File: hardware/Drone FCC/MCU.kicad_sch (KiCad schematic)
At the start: 5 parts, among them U3 STM32F746ZGTx

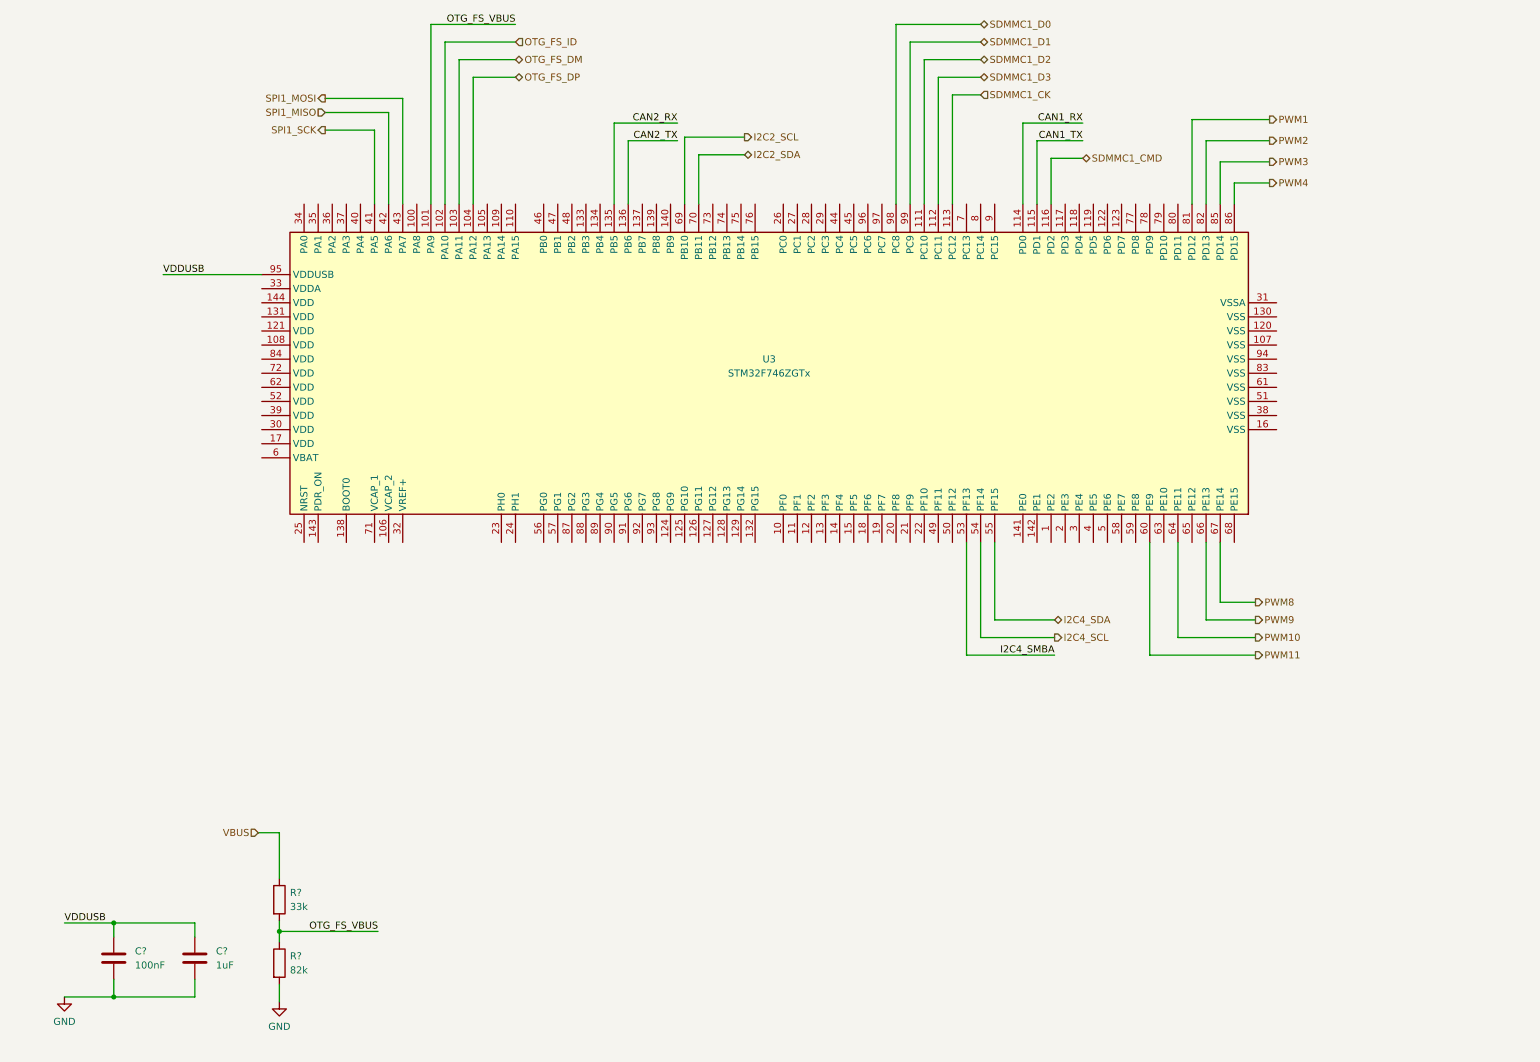
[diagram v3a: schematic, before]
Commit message: finish SWD functional schematic
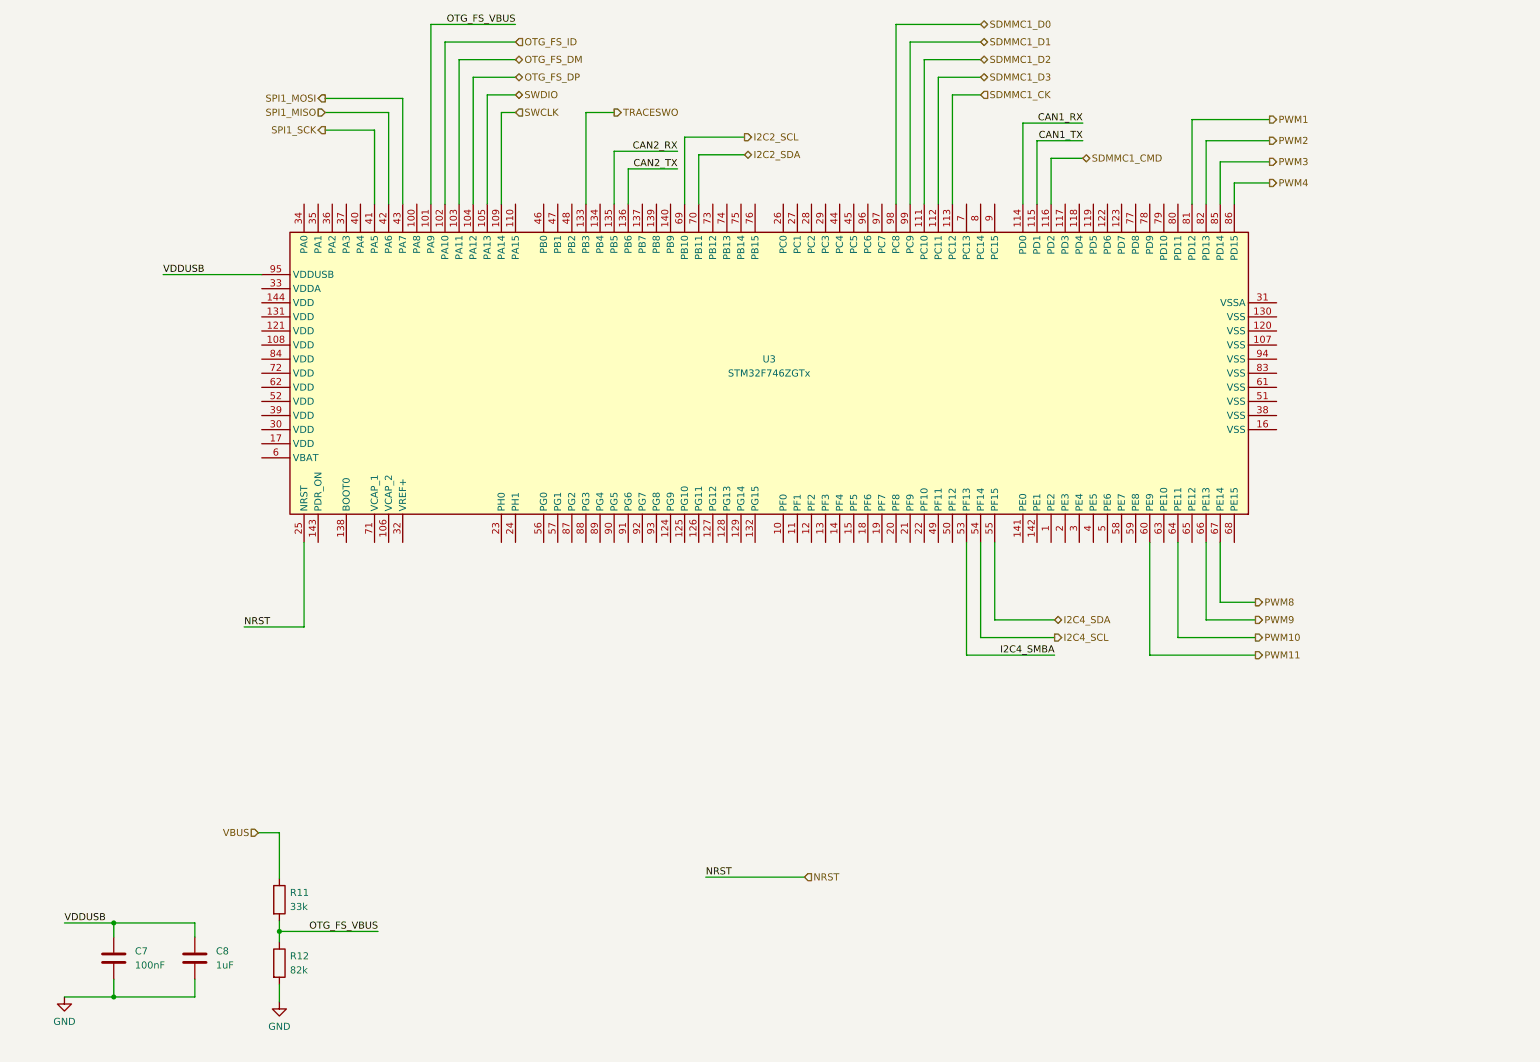
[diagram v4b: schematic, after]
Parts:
- gave numbers to parts that had none: 4
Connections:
- net SWDIO: now reaches U3.105 (PA13)
- net SWCLK: now reaches U3.109 (PA14)
- net TRACESWO: now reaches U3.133 (PB3)
- net NRST: now reaches U3.25 (NRST)
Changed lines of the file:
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@@
-    (stroke (width 0) (type default) (color 0 0 0 0))
-  )
-  (wire (pts (xy 121.285 36.195) (xy 121.285 47.625))
     (stroke (width 0) (type default) (color 0 0 0 0))
   )
@@
     (stroke (width 0) (type default) (color 0 0 0 0))
   )
-  (wire (pts (xy 118.745 33.02) (xy 130.175 33.02))
+  (wire (pts (xy 118.745 38.1) (xy 130.175 38.1))
     (stroke (width 0) (type default) (color 0 0 0 0))
   )
@@
     (stroke (width 0) (type default) (color 0 0 0 0))
   )
+  (wire (pts (xy 100.965 31.115) (xy 98.425 31.115))
+    (stroke (width 0) (type default) (color 0 0 0 0))
+  )
   (wire (pts (xy 100.965 24.765) (xy 93.345 24.765))
     (stroke (width 0) (type default) (color 0 0 0 0))
@@
     (stroke (width 0) (type default) (color 0 0 0 0))
   )
+  (wire (pts (xy 113.665 31.115) (xy 118.745 31.115))
+    (stroke (width 0) (type default) (color 0 0 0 0))
+  )
   (wire (pts (xy 187.325 122.555) (xy 198.12 122.555))
     (stroke (width 0) (type default) (color 0 0 0 0))
@@
     (stroke (width 0) (type default) (color 0 0 0 0))
   )
+  (wire (pts (xy 98.425 31.115) (xy 98.425 47.625))
+    (stroke (width 0) (type default) (color 0 0 0 0))
+  )
+  (wire (pts (xy 113.665 47.625) (xy 113.665 31.115))
+    (stroke (width 0) (type default) (color 0 0 0 0))
+  )
   (wire (pts (xy 88.265 18.415) (xy 100.965 18.415))
     (stroke (width 0) (type default) (color 0 0 0 0))
@@
     (stroke (width 0) (type default) (color 0 0 0 0))
   )
-  (wire (pts (xy 118.745 33.02) (xy 118.745 47.625))
-    (stroke (width 0) (type default) (color 0 0 0 0))
-  )
   (wire (pts (xy 172.085 18.415) (xy 184.785 18.415))
     (stroke (width 0) (type default) (color 0 0 0 0))
@@
     (stroke (width 0) (type default) (color 0 0 0 0))
   )
+  (wire (pts (xy 62.865 123.825) (xy 52.07 123.825))
+    (stroke (width 0) (type default) (color 0 0 0 0))
+  )
+  (wire (pts (xy 62.865 108.585) (xy 62.865 123.825))
+    (stroke (width 0) (type default) (color 0 0 0 0))
+  )
   (wire (pts (xy 184.785 108.585) (xy 184.785 125.73))
     (stroke (width 0) (type default) (color 0 0 0 0))
@@
     (stroke (width 0) (type default) (color 0 0 0 0))
   )
+  (wire (pts (xy 95.885 27.94) (xy 95.885 47.625))
+    (stroke (width 0) (type default) (color 0 0 0 0))
+  )
   (wire (pts (xy 203.2 33.02) (xy 192.405 33.02))
     (stroke (width 0) (type default) (color 0 0 0 0))
   )
+  (wire (pts (xy 100.965 27.94) (xy 95.885 27.94))
+    (stroke (width 0) (type default) (color 0 0 0 0))
+  )
   (wire (pts (xy 43.18 190.5) (xy 43.18 187.325))
     (stroke (width 0) (type default) (color 0 0 0 0))
@@
     (stroke (width 0) (type default) (color 0 0 0 0))
   )
+  (wire (pts (xy 118.745 38.1) (xy 118.745 47.625))
+    (stroke (width 0) (type default) (color 0 0 0 0))
+  )
   (wire (pts (xy 172.085 18.415) (xy 172.085 47.625))
     (stroke (width 0) (type default) (color 0 0 0 0))
@@
     (stroke (width 0) (type default) (color 0 0 0 0))
   )
+  (wire (pts (xy 135.255 168.91) (xy 153.035 168.91))
+    (stroke (width 0) (type default) (color 0 0 0 0))
+  )
   (wire (pts (xy 66.675 34.29) (xy 75.565 34.29))
     (stroke (width 0) (type default) (color 0 0 0 0))
@@
     (stroke (width 0) (type default) (color 0 0 0 0))
   )
-  (wire (pts (xy 121.285 36.195) (xy 130.175 36.195))
+  (wire (pts (xy 121.285 41.275) (xy 130.175 41.275))
     (stroke (width 0) (type default) (color 0 0 0 0))
   )
   (wire (pts (xy 225.425 122.555) (xy 234.315 122.555))
+    (stroke (width 0) (type default) (color 0 0 0 0))
+  )
+  (wire (pts (xy 121.285 41.275) (xy 121.285 47.625))
     (stroke (width 0) (type default) (color 0 0 0 0))
   )
@@
     (effects (font (size 1.27 1.27)) (justify right bottom))
   )
-  (label "CAN2_RX" (at 130.175 33.02 180)
+  (label "CAN2_RX" (at 130.175 38.1 180)
     (effects (font (size 1.27 1.27)) (justify right bottom))
   )
-  (label "CAN2_TX" (at 130.175 36.195 180)
+  (label "CAN2_TX" (at 130.175 41.275 180)
     (effects (font (size 1.27 1.27)) (justify right bottom))
   )
@@
     (effects (font (size 1.27 1.27)) (justify right bottom))
   )
+  (label "NRST" (at 135.255 168.91 0)
+    (effects (font (size 1.27 1.27)) (justify left bottom))
+  )
   (label "VDDUSB" (at 37.465 60.325 0)
     (effects (font (size 1.27 1.27)) (justify left bottom))
   )
+  (label "NRST" (at 52.07 123.825 0)
+    (effects (font (size 1.27 1.27)) (justify left bottom))
+  )
   (label "I2C4_SMBA" (at 198.12 128.905 180)
     (effects (font (size 1.27 1.27)) (justify right bottom))
@@
     (effects (font (size 1.27 1.27)) (justify left))
   )
+  (hierarchical_label "SWDIO" (shape bidirectional) (at 100.965 27.94 0)
+    (effects (font (size 1.27 1.27)) (justify left))
+  )
   (hierarchical_label "SDMMC1_D1" (shape bidirectional) (at 184.785 18.415 0)
     (effects (font (size 1.27 1.27)) (justify left))
@@
     (effects (font (size 1.27 1.27)) (justify left))
   )
+  (hierarchical_label "SWCLK" (shape input) (at 100.965 31.115 0)
+    (effects (font (size 1.27 1.27)) (justify left))
+  )
   (hierarchical_label "SDMMC1_CMD" (shape bidirectional) (at 203.2 39.37 0)
     (effects (font (size 1.27 1.27)) (justify left))
@@
   )
   (hierarchical_label "PWM9" (shape output) (at 234.315 122.555 0)
+    (effects (font (size 1.27 1.27)) (justify left))
+  )
+  (hierarchical_label "TRACESWO" (shape output) (at 118.745 31.115 0)
     (effects (font (size 1.27 1.27)) (justify left))
   )
@@
     (effects (font (size 1.27 1.27)) (justify right))
   )
+  (hierarchical_label "NRST" (shape input) (at 153.035 168.91 0)
+    (effects (font (size 1.27 1.27)) (justify left))
+  )
   (hierarchical_label "PWM8" (shape output) (at 234.315 119.38 0)
     (effects (font (size 1.27 1.27)) (justify left))
@@
   (symbol (lib_id "power:GND") (at 19.685 190.5 0) (unit 1)
     (in_bom yes) (on_board yes) (fields_autoplaced)
-    (property "Reference" "#PWR?" (id 0) (at 19.685 196.85 0)
+    (property "Reference" "#PWR0123" (id 0) (at 19.685 196.85 0)
       (effects (font (size 1.27 1.27)) hide)
     )
@@
   (symbol (lib_id "Device:R") (at 58.42 184.404 0) (unit 1)
     (in_bom yes) (on_board yes) (fields_autoplaced)
-    (property "Reference" "R?" (id 0) (at 60.325 183.1339 0)
+    (property "Reference" "R12" (id 0) (at 60.325 183.1339 0)
       (effects (font (size 1.27 1.27)) (justify left))
     )
@@
   (symbol (lib_id "Device:R") (at 58.42 172.974 0) (unit 1)
     (in_bom yes) (on_board yes) (fields_autoplaced)
-    (property "Reference" "R?" (id 0) (at 60.325 171.7039 0)
+    (property "Reference" "R11" (id 0) (at 60.325 171.7039 0)
       (effects (font (size 1.27 1.27)) (justify left))
     )
@@
   (symbol (lib_id "power:GND") (at 58.42 191.389 0) (unit 1)
     (in_bom yes) (on_board yes) (fields_autoplaced)
-    (property "Reference" "#PWR?" (id 0) (at 58.42 197.739 0)
+    (property "Reference" "#PWR0124" (id 0) (at 58.42 197.739 0)
       (effects (font (size 1.27 1.27)) hide)
     )
@@
   (symbol (lib_id "Device:C") (at 28.575 183.515 0) (unit 1)
     (in_bom yes) (on_board yes) (fields_autoplaced)
-    (property "Reference" "C?" (id 0) (at 32.385 182.2449 0)
+    (property "Reference" "C7" (id 0) (at 32.385 182.2449 0)
       (effects (font (size 1.27 1.27)) (justify left))
     )
@@
   (symbol (lib_id "Device:C") (at 43.18 183.515 0) (unit 1)
     (in_bom yes) (on_board yes) (fields_autoplaced)
-    (property "Reference" "C?" (id 0) (at 46.99 182.2449 0)
+    (property "Reference" "C8" (id 0) (at 46.99 182.2449 0)
       (effects (font (size 1.27 1.27)) (justify left))
     )

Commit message: add HSE and LSE crystals to schematic
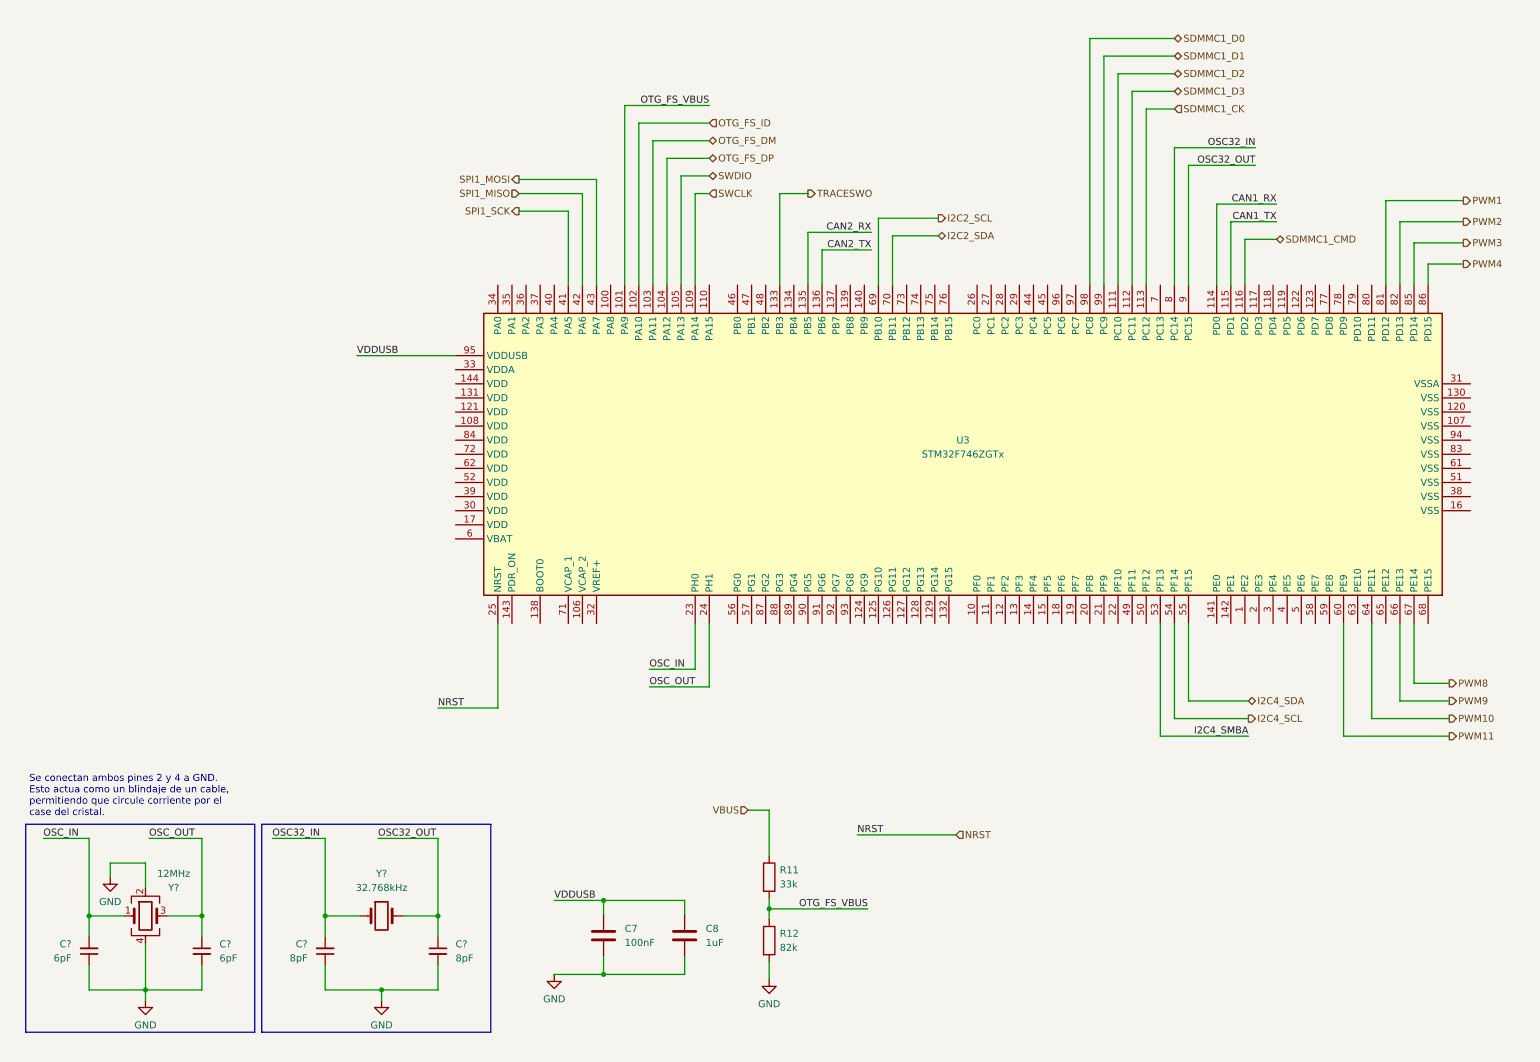
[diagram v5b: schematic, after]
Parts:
- added C? (x2): 6pF, symbol Device:C_Small
- added C? (x2): 8pF, symbol Device:C_Small
- added Y?: 32.768kHz, symbol Device:Crystal
- added Y?: 12MHz, symbol Device:Crystal_GND24
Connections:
- net GND: now also C?.1, C?.1, C?.2, C?.2, Y?.2, Y?.4
- net OSC_IN: now reaches U3.23 (PH0)
- net OSC_IN: now also C?.2, Y?.1
- net OSC_OUT: now reaches U3.24 (PH1)
- net OSC_OUT: now also C?.1, Y?.3
- net OSC32_IN: now reaches U3.8 (PC14)
- net OSC32_IN: now also C?.2, Y?.1
- net OSC32_OUT: now reaches U3.9 (PC15)
- net OSC32_OUT: now also C?.1, Y?.2
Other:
- note added: "Se conectan ambos pines 2 y 4 a GND. Esto actua como un blindaje de un cable, permitiendo que circule corriente por el case del cristal."
- moved on the sheet: C7, C8, R11, R12, U3
